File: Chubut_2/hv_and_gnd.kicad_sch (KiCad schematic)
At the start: 5 parts, among them J24 HighVoltage, J25 HV, J26 GND

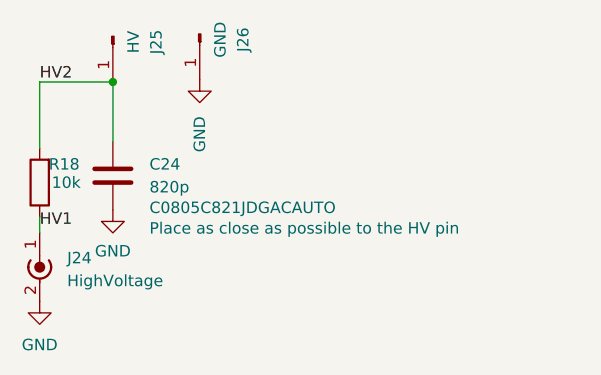
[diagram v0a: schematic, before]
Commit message: Prototype with 4 channels
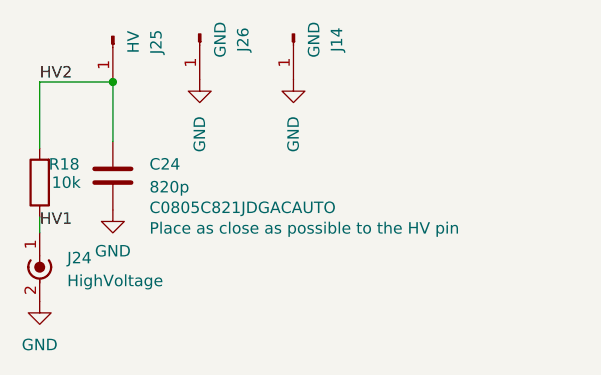
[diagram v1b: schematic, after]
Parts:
- added J14: GND, chubut:MILL-MAX_0965-0-15-20-80-14-11-0, symbol Connector:Conn_01x01_Male
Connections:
- net GND: now also J14.1 (Pin_1)
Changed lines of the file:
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@@
+    (pin "1")
+  )
+  (symbol (lib_id "power:GND") (at 161.544 107.188 0) (unit 1)
+    (in_bom yes) (on_board yes) (fields_autoplaced)
+    (property "Reference" "#PWR037" (id 0) (at 161.544 113.538 0)
+      (effects (font (size 1.27 1.27)) hide)
+    )
+    (property "Value" "GND" (id 1) (at 161.5441 111.252 90)
+      (effects (font (size 1.27 1.27)) (justify right))
+    )
+    (property "Footprint" "" (id 2) (at 161.544 107.188 0)
+      (effects (font (size 1.27 1.27)) hide)
+    )
+    (property "Datasheet" "" (id 3) (at 161.544 107.188 0)
+      (effects (font (size 1.27 1.27)) hide)
+    )
+    (pin "1")
+  )
+  (symbol (lib_id "Connector:Conn_01x01_Male") (at 161.544 102.108 270) (unit 1)
+    (in_bom yes) (on_board yes) (fields_autoplaced)
+    (property "Reference" "J14" (id 0) (at 166.37 102.743 0))
+    (property "Value" "GND" (id 1) (at 163.83 102.743 0))
+    (property "Footprint" "chubut:MILL-MAX_0965-0-15-20-80-14-11-0" (id 2) (at 161.544 102.108 0)
+      (effects (font (size 1.27 1.27)) hide)
+    )
+    (property "Datasheet" "https://www.mill-max.com/products/pin/0965/0965-0-15-20-80-14-11-0?s_term=0965-0-15-20-80-14-11-0&s_type=Quick%2FProduct%2FPart+Number+Search" (id 3) (at 161.544 102.108 0)
+      (effects (font (size 1.27 1.27)) hide)
+    )
+    (property "Manufacturer number" "0965-0-15-20-80-14-11-0" (id 4) (at 161.544 102.108 0)
+      (effects (font (size 1.27 1.27)) hide)
+    )
+    (property "Manufacturer" "Mill-Max Manufacturing Corp." (id 5) (at 161.544 102.108 0)
+      (effects (font (size 1.27 1.27)) hide)
+    )
     (pin "1")
   )

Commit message: Minor fixes
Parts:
- renumbered C24 to C14, J24 to J11, J25 to J12, J26 to J13, R18 to R9
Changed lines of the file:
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@@
   (symbol (lib_id "Connector:Conn_01x01_Male") (at 141.478 102.362 270) (unit 1)
     (in_bom yes) (on_board yes)
-    (property "Reference" "J25" (id 0) (at 146.304 102.997 0))
+    (property "Reference" "J12" (id 0) (at 146.304 102.997 0))
     (property "Value" "HV" (id 1) (at 143.764 102.997 0))
     (property "Footprint" "chubut:MILL-MAX_0965-0-15-20-80-14-11-0" (id 2) (at 141.478 102.362 0)
@@
   (symbol (lib_id "Connector:Conn_Coaxial_Power") (at 133.35 126.746 0) (unit 1)
     (in_bom yes) (on_board yes) (fields_autoplaced)
-    (property "Reference" "J24" (id 0) (at 136.398 126.9999 0)
+    (property "Reference" "J11" (id 0) (at 136.398 126.9999 0)
       (effects (font (size 1.27 1.27)) (justify left))
     )
@@
   (symbol (lib_id "Device:C") (at 141.478 117.856 0) (unit 1)
     (in_bom yes) (on_board yes)
-    (property "Reference" "C24" (id 0) (at 145.542 116.5859 0)
+    (property "Reference" "C14" (id 0) (at 145.542 116.5859 0)
       (effects (font (size 1.27 1.27)) (justify left))
     )
@@
   (symbol (lib_id "power:GND") (at 133.35 131.826 0) (unit 1)
     (in_bom yes) (on_board yes) (fields_autoplaced)
-    (property "Reference" "#PWR063" (id 0) (at 133.35 138.176 0)
+    (property "Reference" "#PWR034" (id 0) (at 133.35 138.176 0)
       (effects (font (size 1.27 1.27)) hide)
     )
@@
   (symbol (lib_id "Connector:Conn_01x01_Male") (at 151.13 102.108 270) (unit 1)
     (in_bom yes) (on_board yes) (fields_autoplaced)
-    (property "Reference" "J26" (id 0) (at 155.956 102.743 0))
+    (property "Reference" "J13" (id 0) (at 155.956 102.743 0))
     (property "Value" "GND" (id 1) (at 153.416 102.743 0))
     (property "Footprint" "chubut:MILL-MAX_0965-0-15-20-80-14-11-0" (id 2) (at 151.13 102.108 0)
@@
   (symbol (lib_id "Device:R") (at 133.35 118.618 180) (unit 1)
     (in_bom yes) (on_board yes)
-    (property "Reference" "R18" (id 0) (at 136.0678 116.586 0))
+    (property "Reference" "R9" (id 0) (at 136.0678 116.586 0))
     (property "Value" "10k" (id 1) (at 136.2964 118.618 0))
     (property "Footprint" "Resistor_SMD:R_0805_2012Metric_Pad1.20x1.40mm_HandSolder" (id 2) (at 135.128 118.618 90)
@@
   (symbol (lib_id "power:GND") (at 141.478 121.666 0) (unit 1)
     (in_bom yes) (on_board yes) (fields_autoplaced)
-    (property "Reference" "#PWR064" (id 0) (at 141.478 128.016 0)
+    (property "Reference" "#PWR035" (id 0) (at 141.478 128.016 0)
       (effects (font (size 1.27 1.27)) hide)
     )
@@
   (symbol (lib_id "power:GND") (at 151.13 107.188 0) (unit 1)
     (in_bom yes) (on_board yes) (fields_autoplaced)
-    (property "Reference" "#PWR065" (id 0) (at 151.13 113.538 0)
+    (property "Reference" "#PWR036" (id 0) (at 151.13 113.538 0)
       (effects (font (size 1.27 1.27)) hide)
     )

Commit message: New version with shieldings and the other suggestions from the workshop
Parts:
- renumbered J11 to J15, J12 to J16, J13 to J17, J14 to J18
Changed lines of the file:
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@@
   (symbol (lib_id "Connector:Conn_01x01_Male") (at 141.478 102.362 270) (unit 1)
     (in_bom yes) (on_board yes)
-    (property "Reference" "J12" (id 0) (at 146.304 102.997 0))
+    (property "Reference" "J16" (id 0) (at 146.304 102.997 0))
     (property "Value" "HV" (id 1) (at 143.764 102.997 0))
     (property "Footprint" "chubut:MILL-MAX_0965-0-15-20-80-14-11-0" (id 2) (at 141.478 102.362 0)
@@
   (symbol (lib_id "Connector:Conn_Coaxial_Power") (at 133.35 126.746 0) (unit 1)
     (in_bom yes) (on_board yes) (fields_autoplaced)
-    (property "Reference" "J11" (id 0) (at 136.398 126.9999 0)
+    (property "Reference" "J15" (id 0) (at 136.398 126.9999 0)
       (effects (font (size 1.27 1.27)) (justify left))
     )
@@
   (symbol (lib_id "power:GND") (at 133.35 131.826 0) (unit 1)
     (in_bom yes) (on_board yes) (fields_autoplaced)
-    (property "Reference" "#PWR034" (id 0) (at 133.35 138.176 0)
+    (property "Reference" "#PWR040" (id 0) (at 133.35 138.176 0)
       (effects (font (size 1.27 1.27)) hide)
     )
@@
   (symbol (lib_id "Connector:Conn_01x01_Male") (at 151.13 102.108 270) (unit 1)
     (in_bom yes) (on_board yes) (fields_autoplaced)
-    (property "Reference" "J13" (id 0) (at 155.956 102.743 0))
+    (property "Reference" "J17" (id 0) (at 155.956 102.743 0))
     (property "Value" "GND" (id 1) (at 153.416 102.743 0))
     (property "Footprint" "chubut:MILL-MAX_0965-0-15-20-80-14-11-0" (id 2) (at 151.13 102.108 0)
@@
   (symbol (lib_id "power:GND") (at 141.478 121.666 0) (unit 1)
     (in_bom yes) (on_board yes) (fields_autoplaced)
-    (property "Reference" "#PWR035" (id 0) (at 141.478 128.016 0)
+    (property "Reference" "#PWR041" (id 0) (at 141.478 128.016 0)
       (effects (font (size 1.27 1.27)) hide)
     )
@@
   (symbol (lib_id "power:GND") (at 151.13 107.188 0) (unit 1)
     (in_bom yes) (on_board yes) (fields_autoplaced)
-    (property "Reference" "#PWR036" (id 0) (at 151.13 113.538 0)
+    (property "Reference" "#PWR042" (id 0) (at 151.13 113.538 0)
       (effects (font (size 1.27 1.27)) hide)
     )
@@
   (symbol (lib_id "power:GND") (at 161.544 107.188 0) (unit 1)
     (in_bom yes) (on_board yes) (fields_autoplaced)
-    (property "Reference" "#PWR037" (id 0) (at 161.544 113.538 0)
+    (property "Reference" "#PWR043" (id 0) (at 161.544 113.538 0)
       (effects (font (size 1.27 1.27)) hide)
     )
@@
   (symbol (lib_id "Connector:Conn_01x01_Male") (at 161.544 102.108 270) (unit 1)
     (in_bom yes) (on_board yes) (fields_autoplaced)
-    (property "Reference" "J14" (id 0) (at 166.37 102.743 0))
+    (property "Reference" "J18" (id 0) (at 166.37 102.743 0))
     (property "Value" "GND" (id 1) (at 163.83 102.743 0))
     (property "Footprint" "chubut:MILL-MAX_0965-0-15-20-80-14-11-0" (id 2) (at 161.544 102.108 0)
